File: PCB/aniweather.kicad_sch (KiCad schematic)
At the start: 35 parts, among them SW1 SW_DIP_x01, SW2 SW_Push, SW3 SW_Push, U5 TPS63001

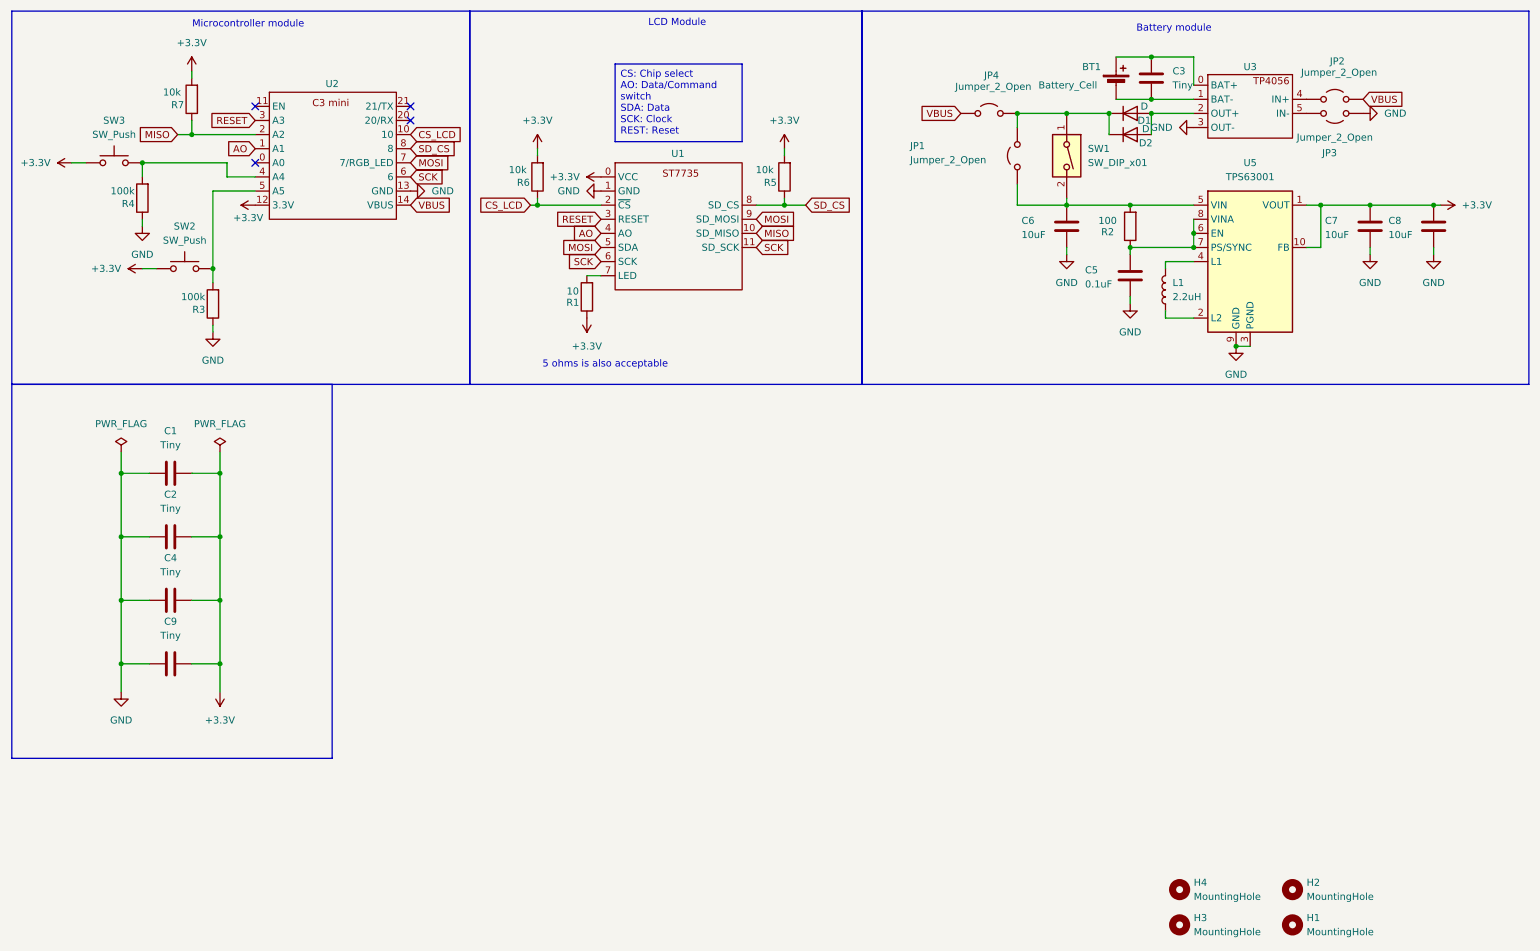
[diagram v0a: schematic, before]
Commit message: Priority Power MUX
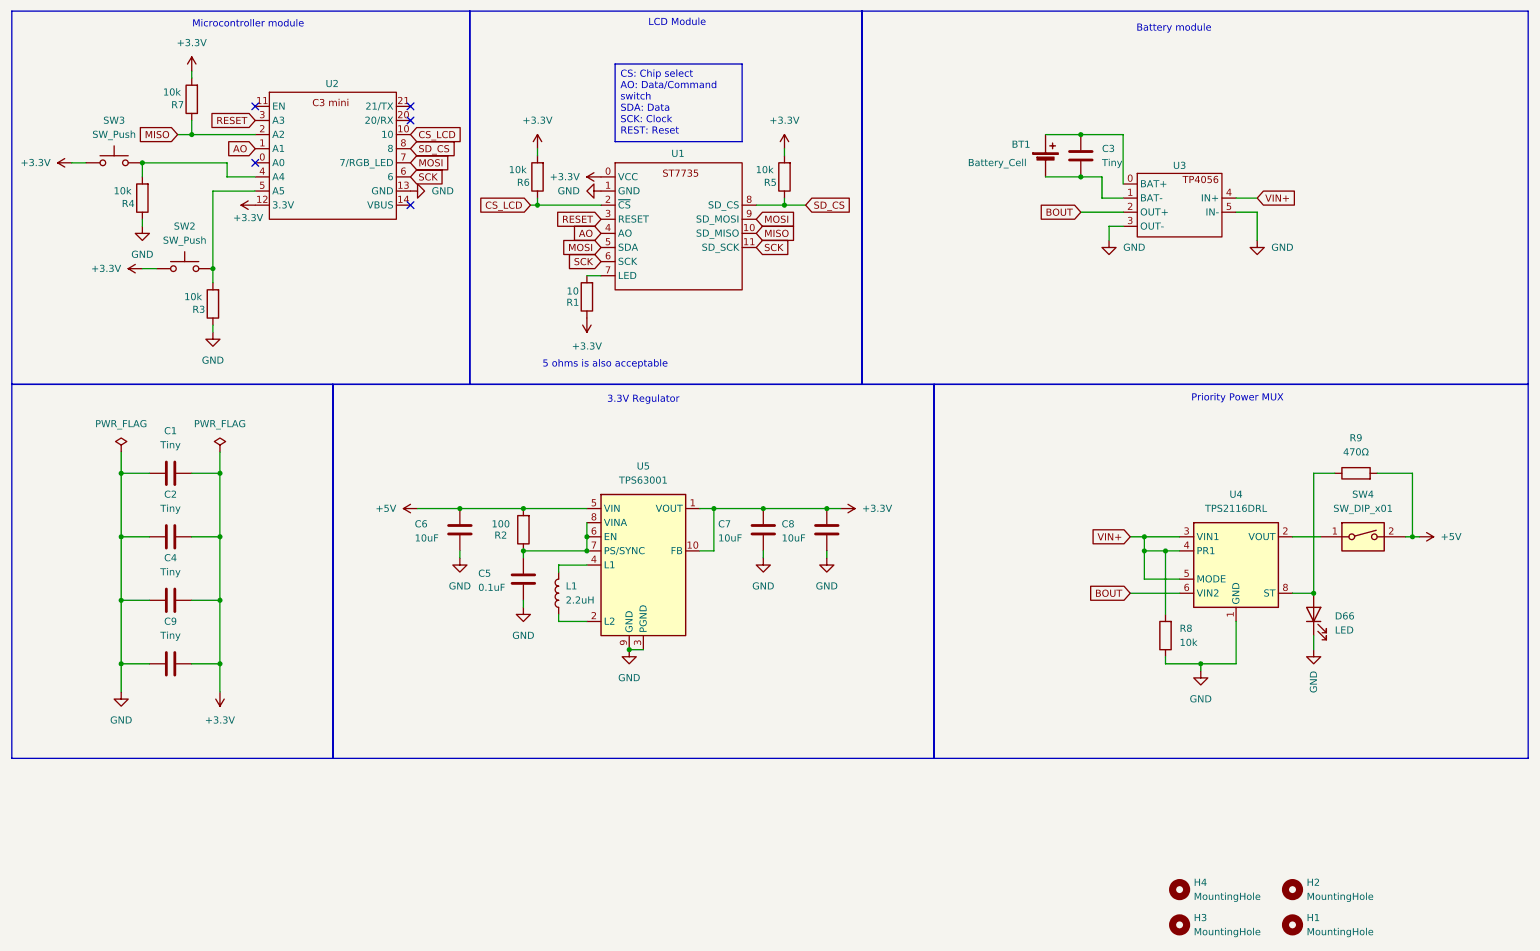
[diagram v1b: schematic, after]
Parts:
- removed D1, D2: D, Diode_THT:D_DO-35_SOD27_P7.62mm_Horizontal, symbol Device:D
- removed JP1, JP2, JP3, JP4: Jumper_2_Open, Jumper:SolderJumper-2_P1.3mm_Open_Pad1.0x1.5mm, symbol Jumper:Jumper_2_Open
- removed SW1: SW_DIP_x01, Button_Switch_THT:SW_DIP_SPSTx01_Slide_9.78x4.72mm_W7.62mm_P2.54mm, symbol Switch:SW_DIP_x01
- added D66: LED, LED_SMD:LED_0603_1608Metric_Pad1.05x0.95mm_HandSolder, symbol Device:LED
- added R8: 10k, Resistor_THT:R_Axial_DIN0207_L6.3mm_D2.5mm_P10.16mm_Horizontal, symbol Device:R
- added R9: 470Ω, Resistor_THT:R_Axial_DIN0207_L6.3mm_D2.5mm_P10.16mm_Horizontal, symbol Device:R
- added SW4: SW_DIP_x01, Button_Switch_THT:SW_DIP_SPSTx01_Slide_9.78x4.72mm_W7.62mm_P2.54mm, symbol Switch:SW_DIP_x01
- added U4: TPS2116DRL, Package_TO_SOT_SMD:SOT-583-8, symbol Power_Management:TPS2116DRL
- C6, C7, C8: footprint Capacitor_THT:C_Disc_D5.0mm_W2.5mm_P2.50mm -> Capacitor_SMD:C_0805_2012Metric_Pad1.18x1.45mm_HandSolder
- R3, R4: value 100k -> 10k
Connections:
- net GND: now also U3.5 (IN-), D66.1 (K), R8.1, U4.1 (GND)
- net +5V: now reaches C6.1, R2.2, U5.5 (VIN)
- net +5V: now also R9.2, SW4.2
- net BOUT: now reaches U3.2 (OUT+)
- net BOUT: now also U4.6 (VIN2)
- net VIN+: now reaches U3.4 (IN+)
- net VIN+: now also R8.2, U4.3 (VIN1), U4.4 (PR1), U4.5 (MODE)
- net VBUS: no longer names the net of U2.14 (VBUS)
- new net: SW4.1, U4.2 (VOUT), U4.7 (VOUT)
- new net: D66.2 (A), R9.1, U4.8 (ST)
- no-connect marks 4 -> 5
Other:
- note added: "3.3V Regulator"
- note added: "Priority Power MUX"
- moved on the sheet: BT1, C3, C5, C6, C7, C8, L1, R2, U3, U5

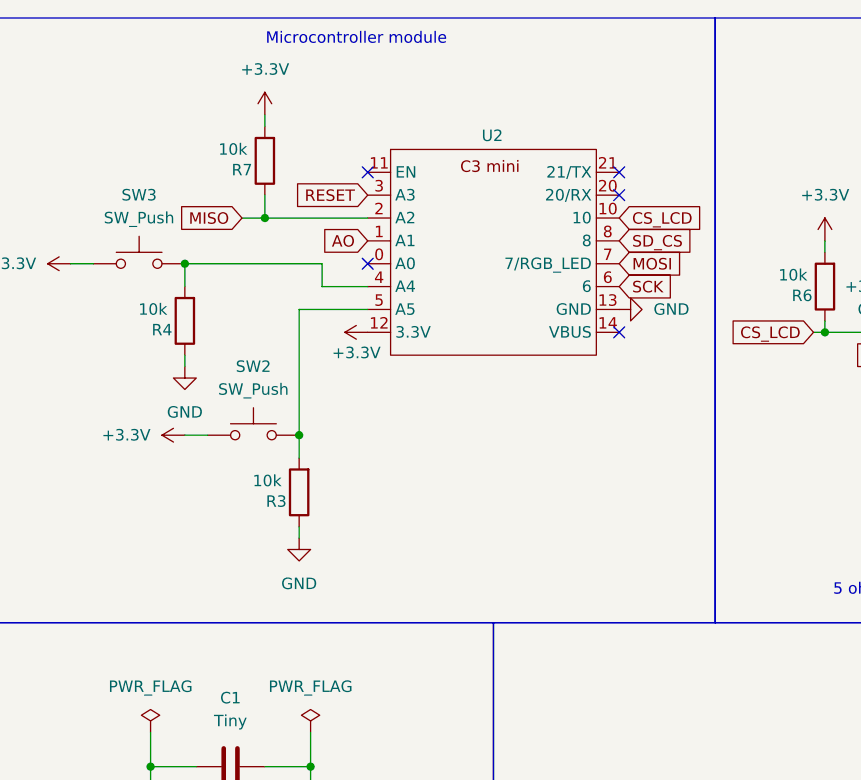
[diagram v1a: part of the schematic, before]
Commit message: FIX MISO and MOSI order
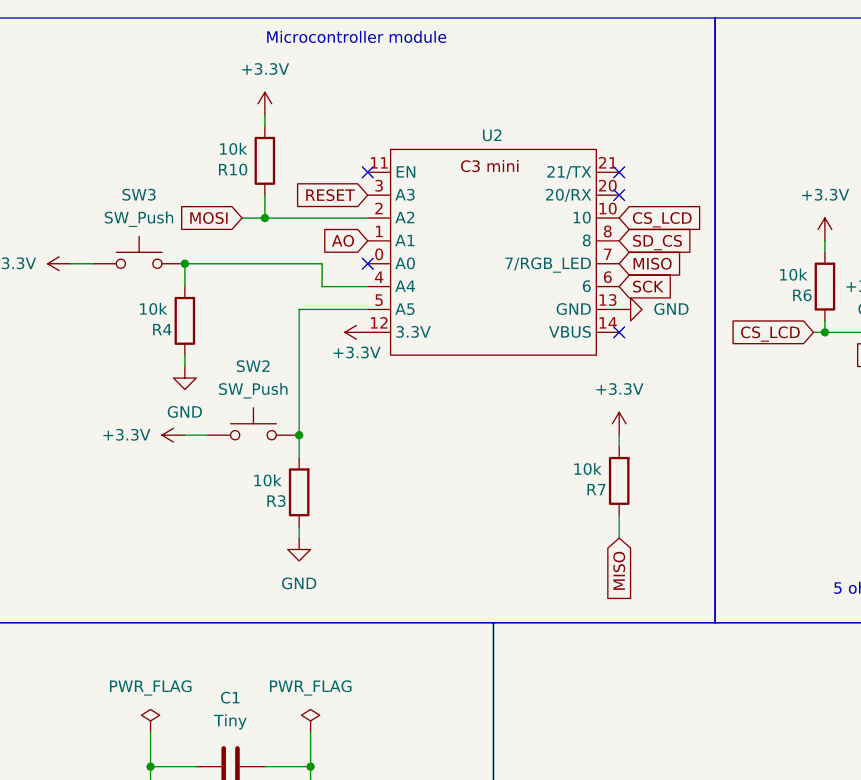
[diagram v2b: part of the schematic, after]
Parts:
- added R10: 10k, Resistor_THT:R_Axial_DIN0207_L6.3mm_D2.5mm_P10.16mm_Horizontal, symbol Device:R
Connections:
- net +3.3V: now also R10.2
- net MISO: now also U2.7 (7/RGB_LED); no longer U2.2 (A2)
- net MOSI: now also U2.2 (A2), R10.1; no longer U2.7 (7/RGB_LED)
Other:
- moved on the sheet: R7
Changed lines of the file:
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@@
 	(wire
 		(pts
+			(xy 83.82 67.31) (xy 83.82 69.85)
+		)
+		(stroke
+			(width 0)
+			(type default)
+		)
+	)
+	(wire
+		(pts
 			(xy 115.57 106.68) (xy 115.57 109.22)
 		)
@@
 	(wire
 		(pts
+			(xy 83.82 58.42) (xy 83.82 59.69)
+		)
+		(stroke
+			(width 0)
+			(type default)
+		)
+	)
+	(wire
+		(pts
 			(xy 215.9 114.3) (xy 215.9 109.22)
 		)
@@
 		)
 	)
-	(global_label "MOSI"
+	(global_label "MISO"
 		(shape input)
-		(at 83.82 39.37 0)
+		(at 83.82 69.85 270)
 		(fields_autoplaced yes)
 		(effects
@@
 				(size 1.27 1.27)
 			)
-			(justify left)
+			(justify right)
 		)
 		(property "Intersheetrefs" "${INTERSHEET_REFS}"
-			(at 91.4014 39.37 0)
+			(at 83.82 77.4314 90)
 			(effects
 				(font
 					(size 1.27 1.27)
 				)
-				(justify left)
+				(justify right)
 				(hide yes)
 			)
@@
 	(global_label "MISO"
 		(shape input)
+		(at 83.82 39.37 0)
+		(fields_autoplaced yes)
+		(effects
+			(font
+				(size 1.27 1.27)
+			)
+			(justify left)
+		)
+		(property "Intersheetrefs" "${INTERSHEET_REFS}"
+			(at 91.4014 39.37 0)
+			(effects
+				(font
+					(size 1.27 1.27)
+				)
+				(justify left)
+				(hide yes)
+			)
+		)
+	)
+	(global_label "MOSI"
+		(shape input)
 		(at 41.91 34.29 180)
 		(fields_autoplaced yes)
@@
 	)
 	(symbol
+		(lib_id "Device:R")
+		(at 44.45 27.94 180)
+		(unit 1)
+		(exclude_from_sim no)
+		(in_bom yes)
+		(on_board yes)
+		(dnp no)
+		(property "Reference" "R10"
+			(at 40.894 28.956 0)
+			(effects
+				(font
+					(size 1.27 1.27)
+				)
+			)
+		)
+		(property "Value" "10k"
+			(at 40.894 26.67 0)
+			(effects
+				(font
+					(size 1.27 1.27)
+				)
+			)
+		)
+		(property "Footprint" "Resistor_THT:R_Axial_DIN0207_L6.3mm_D2.5mm_P10.16mm_Horizontal"
+			(at 46.228 27.94 90)
+			(effects
+				(font
+					(size 1.27 1.27)
+				)
+				(hide yes)
+			)
+		)
+		(property "Datasheet" "~"
+			(at 44.45 27.94 0)
+			(effects
+				(font
+					(size 1.27 1.27)
+				)
+				(hide yes)
+			)
+		)
+		(property "Description" "Resistor"
+			(at 44.45 27.94 0)
+			(effects
+				(font
+					(size 1.27 1.27)
+				)
+				(hide yes)
+			)
+		)
+		(pin "1"
+		)
+		(pin "2"
+		)
+		(instances
+			(project "aniweather"
+				(path "/e7e4d5de-a607-486c-961b-1d24c88fafef"
+					(reference "R10")
+					(unit 1)
+				)
+			)
+		)
+	)
+	(symbol
 		(lib_id "power:GND")
 		(at 83.82 44.45 90)
@@
 	(symbol
 		(lib_id "Device:R")
-		(at 44.45 27.94 180)
+		(at 83.82 63.5 180)
 		(unit 1)
 		(exclude_from_sim no)
@@
 		(dnp no)
 		(property "Reference" "R7"
-			(at 41.91 28.956 0)
+			(at 81.28 64.516 0)
 			(effects
 				(font
@@
 		)
 		(property "Value" "10k"
-			(at 40.894 26.67 0)
+			(at 80.264 62.23 0)
 			(effects
 				(font
@@
 		)
 		(property "Footprint" "Resistor_THT:R_Axial_DIN0207_L6.3mm_D2.5mm_P10.16mm_Horizontal"
-			(at 46.228 27.94 90)
+			(at 85.598 63.5 90)
 			(effects
 				(font
@@
 		)
 		(property "Datasheet" "~"
-			(at 44.45 27.94 0)
+			(at 83.82 63.5 0)
 			(effects
 				(font
@@
 		)
 		(property "Description" "Resistor"
-			(at 44.45 27.94 0)
+			(at 83.82 63.5 0)
 			(effects
 				(font
@@
 					(unit 1)
 				)
+			)
+		)
+	)
+	(symbol
+		(lib_id "power:+3.3V")
+		(at 83.82 58.42 0)
+		(unit 1)
+		(exclude_from_sim no)
+		(in_bom yes)
+		(on_board yes)
+		(dnp no)
+		(fields_autoplaced yes)
+		(property "Reference" "#PWR026"
+			(at 83.82 62.23 0)
+			(effects
+				(font
+					(size 1.27 1.27)
+				)
+				(hide yes)
+			)
+		)
+		(property "Value" "+3.3V"
+			(at 83.82 53.34 0)
+			(effects
+				(font
+					(size 1.27 1.27)
+				)
+			)
+		)
+		(property "Footprint" ""
+			(at 83.82 58.42 0)
+			(effects
+				(font
+					(size 1.27 1.27)
+				)
+				(hide yes)
+			)
+		)
+		(property "Datasheet" ""
+			(at 83.82 58.42 0)
+			(effects
+				(font
+					(size 1.27 1.27)
+				)
+				(hide yes)
+			)
+		)
+		(property "Description" "Power symbol creates a global label with name \"+3.3V\""
+			(at 83.82 58.42 0)
+			(effects
+				(font
+					(size 1.27 1.27)
+				)
+				(hide yes)
+			)
+		)
+		(pin "1"
+		)
+		(instances
+			(project "aniweather"
+				(path "/e7e4d5de-a607-486c-961b-1d24c88fafef"
+					(reference "#PWR026")
+					(unit 1)
+				)

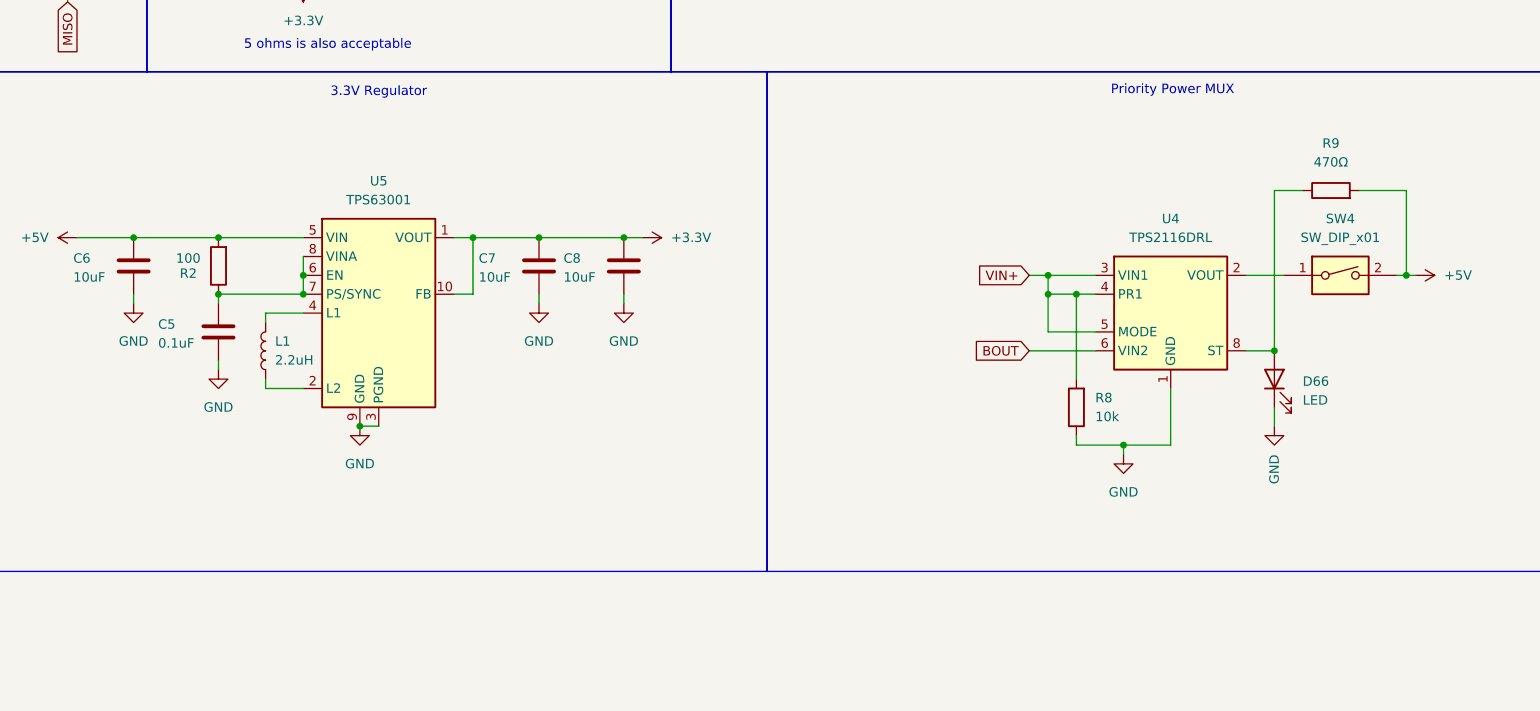
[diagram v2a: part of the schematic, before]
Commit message: Use SMD resistors
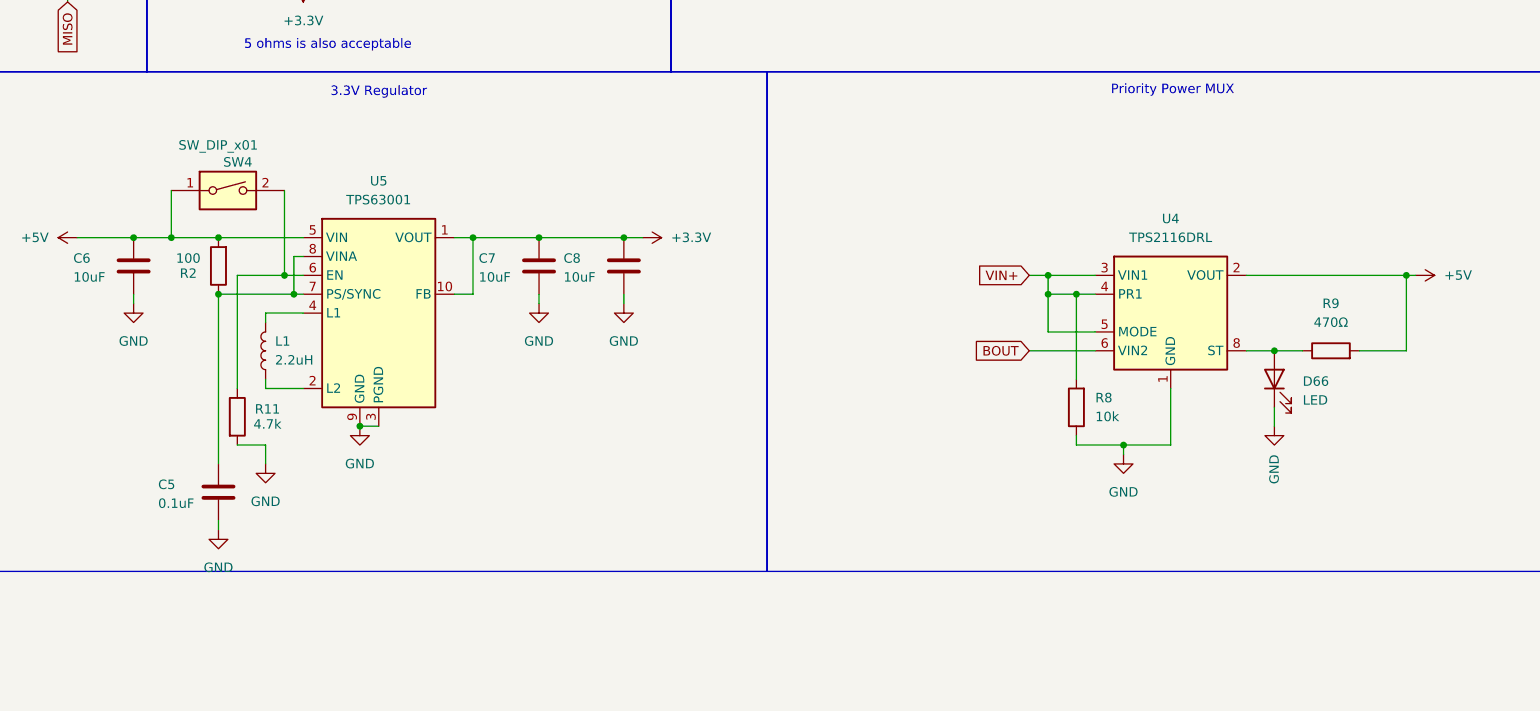
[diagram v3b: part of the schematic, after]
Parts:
- added R11: 4.7k, Resistor_SMD:R_0805_2012Metric_Pad1.20x1.40mm_HandSolder, symbol Device:R
- C1, C2, C3, C4, C5, C9: footprint Capacitor_THT:C_Disc_D5.0mm_W2.5mm_P2.50mm -> Capacitor_SMD:C_0805_2012Metric_Pad1.18x1.45mm_HandSolder
- R1, R10, R2, R3, R4, R5, R6, R7, R8, R9: footprint Resistor_THT:R_Axial_DIN0207_L6.3mm_D2.5mm_P10.16mm_Horizontal -> Resistor_SMD:R_0805_2012Metric_Pad1.20x1.40mm_HandSolder
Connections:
- net +5V: now also SW4.1, U4.2 (VOUT), U4.7 (VOUT); no longer SW4.2
- net GND: now also R11.2
- net at C5.1, R2.1, U5.7 (PS/SYNC)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: no longer U5.6 (EN)
- new net: R11.1, SW4.2, U5.6 (EN)
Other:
- moved on the sheet: C5, R9, SW4
